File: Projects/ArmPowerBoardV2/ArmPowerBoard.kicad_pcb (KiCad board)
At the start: 2 copper layers, 130 x 65.2 mm, 14 parts, among them J1 22V Output, J2 12V Output, P1 BATT_CON, U1 IQL24040A050V-009-R-ND

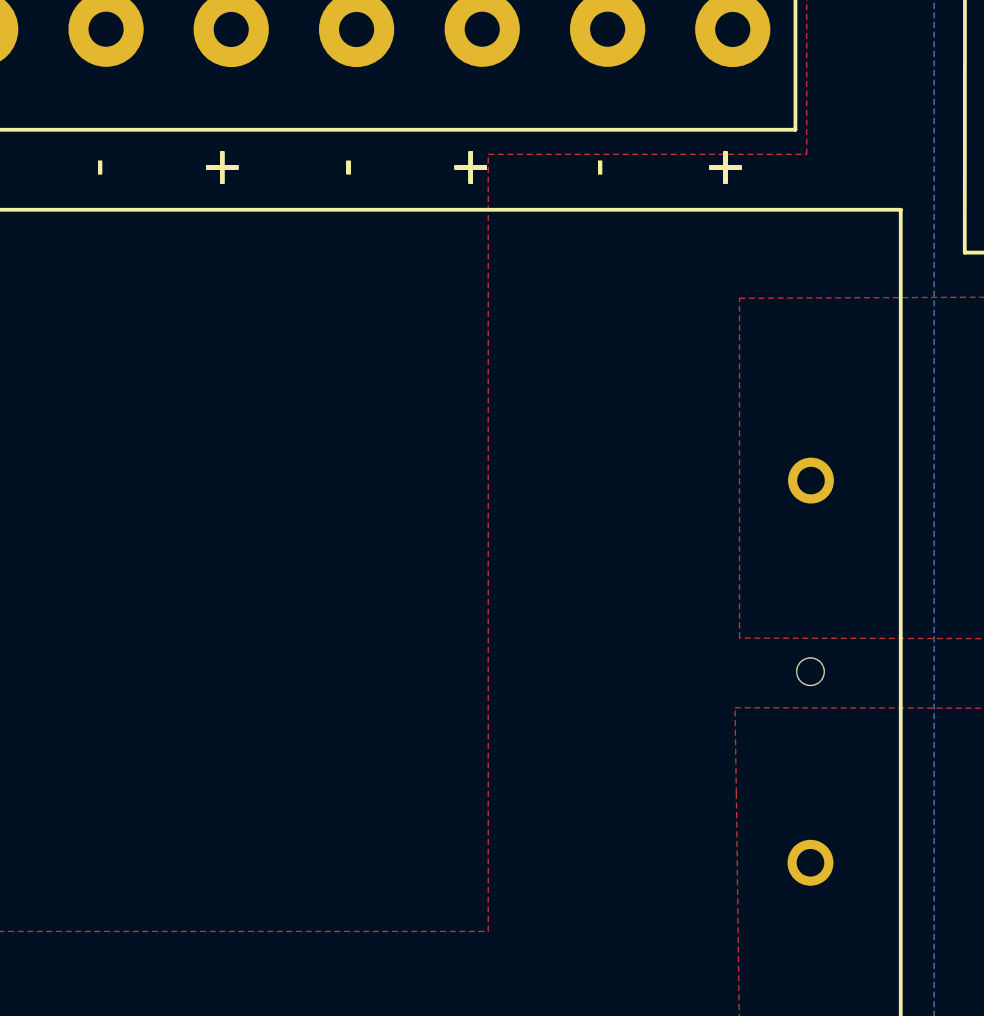
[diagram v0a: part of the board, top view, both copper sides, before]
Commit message: The on/off switch is conncted to power
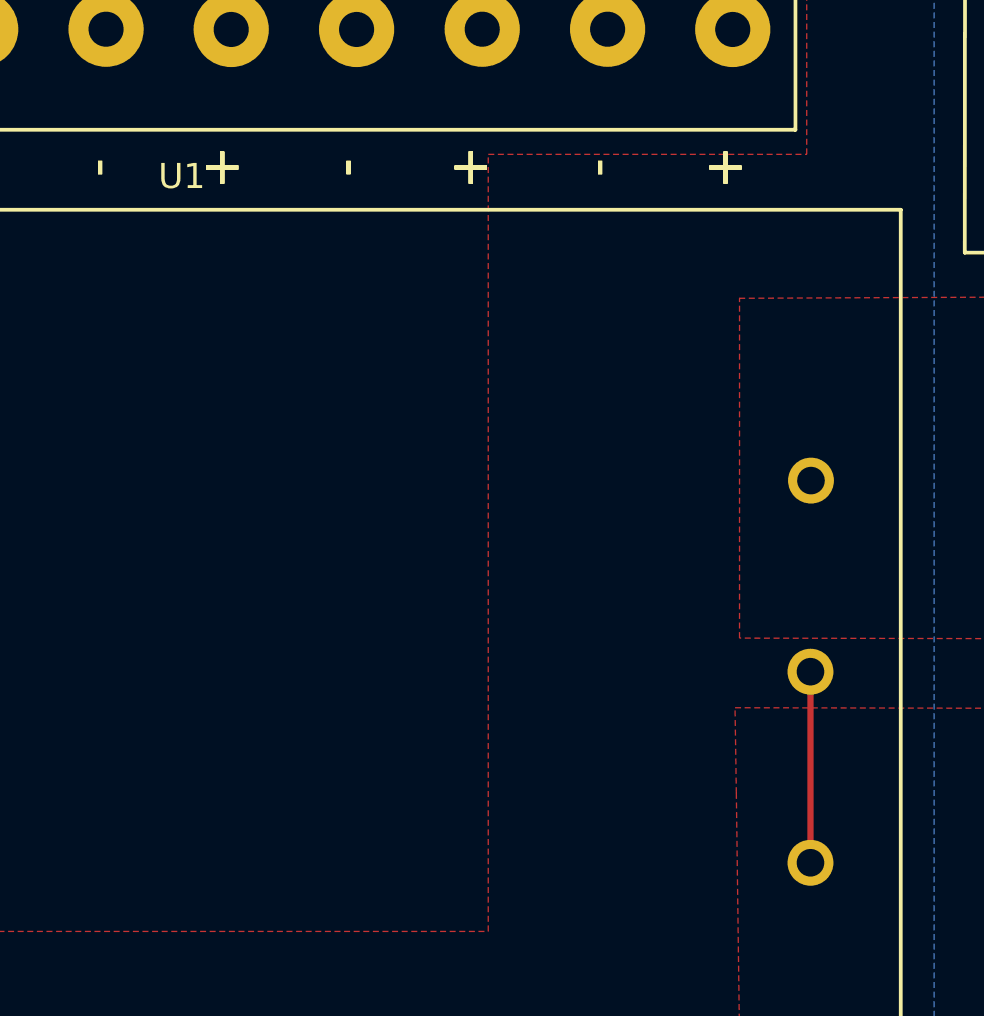
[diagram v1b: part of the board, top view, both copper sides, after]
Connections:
- 9.31kR pad 1: (no net) -> Net-(0.27-Pad2)
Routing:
- net Net-(P1-Pad2): track 0.00 -> 7.62 mm
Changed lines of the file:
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@@
 (kicad_pcb (version 4) (host pcbnew 4.0.7)
   (general
-    (links 0)
+    (links 52)
     (no_connects 0)
-    (area 48.224999 104.724999 178.375001 166.075001)
+    (area 48.224999 102.724999 178.375001 168.075001)
     (thickness 1.6)
     (drawings 33)
-    (tracks 103)
+    (tracks 105)
     (zones 0)
     (modules 14)
@@
     (mod_text_size 1 1)
     (mod_text_width 0.15)
-    (pad_size 3.2 3.2)
-    (pad_drill 3.2)
+    (pad_size 2.59 2.59)
+    (pad_drill 1.7)
     (pad_to_mask_clearance 0.2)
     (aux_axis_origin 0 0)
@@
       (net 6 "Net-(P1-Pad2)"))
   )
-  (module USST-footprints:IQL24040A050V_Power_Supply (layer F.Cu)
-    (at 81.1887 149.662 180)
-    (fp_text reference U1 (at -25.73 27.37 180) (layer F.SilkS) hide
-      (effects (font (size 1 1) (thickness 0.15)))
-    )
-    (fp_text value IQL24040A050V-009-R-ND (at -25.82 24.43 180) (layer F.Fab)
-      (effects (font (size 1 1) (thickness 0.15)))
-    )
-    (fp_line (start -54.36 -10.77) (end 3.6 -10.8) (layer F.SilkS) (width 0.15))
-    (fp_line (start 3.6 -10.8) (end 3.6 26.04) (layer F.SilkS) (width 0.15))
-    (fp_line (start 3.6 26.04) (end -54.4 26.04) (layer F.SilkS) (width 0.15))
-    (fp_line (start -54.4 26.04) (end -54.4 -10.8) (layer F.SilkS) (width 0.15))
-    (pad 8 thru_hole circle (at 0 0 180) (size 2.59 2.59) (drill 1.7) (layers *.Cu *.Mask)
-      (net 3 "Net-(0.27-Pad2)"))
-    (pad 4 thru_hole circle (at 0 15.29 180) (size 2.59 2.59) (drill 1.7) (layers *.Cu *.Mask)
-      (net 1 /-Vout))
-    (pad 7 thru_hole circle (at 0 3.81 180) (size 1.83 1.83) (drill 1.1) (layers *.Cu *.Mask)
-      (net 3 "Net-(0.27-Pad2)"))
-    (pad 6 thru_hole circle (at 0 7.62 180) (size 1.83 1.83) (drill 1.1) (layers *.Cu *.Mask)
-      (net 4 "Net-(9.3182-Pad2)"))
-    (pad 8 thru_hole circle (at 0 11.43 180) (size 1.83 1.83) (drill 1.1) (layers *.Cu *.Mask)
-      (net 3 "Net-(0.27-Pad2)"))
-    (pad 1 thru_hole circle (at -50.8 0 180) (size 1.83 1.83) (drill 1.1) (layers *.Cu *.Mask)
-      (net 6 "Net-(P1-Pad2)"))
-    (pad "" np_thru_hole circle (at -50.8 7.62 180) (size 1.1 1.1) (drill 1.1) (layers *.Cu *.Mask))
-    (pad 3 thru_hole circle (at -50.82 15.24 180) (size 1.83 1.83) (drill 1.1) (layers *.Cu *.Mask)
-      (net 5 GND))
-  )
   (module Resistors_SMD:R_1812 (layer F.Cu)
     (at 73.05984 132.904538)
@@
     (fp_line (start 0.6 0.875) (end -0.6 0.875) (layer F.SilkS) (width 0.15))
     (fp_line (start -0.6 -0.875) (end 0.6 -0.875) (layer F.SilkS) (width 0.15))
-    (pad 1 smd rect (at -0.95 0 90) (size 0.7 1.3) (layers F.Cu F.Paste F.Mask))
+    (pad 1 smd rect (at -0.95 0 90) (size 0.7 1.3) (layers F.Cu F.Paste F.Mask)
+      (net 3 "Net-(0.27-Pad2)"))
     (pad 2 smd rect (at 0.95 0 90) (size 0.7 1.3) (layers F.Cu F.Paste F.Mask)
       (net 4 "Net-(9.3182-Pad2)"))
@@
       (net 24 "Net-(USB1-Pad18)"))
   )
+  (module USST-footprints:IQL24040A050V_Power_Supply (layer F.Cu)
+    (at 81.1887 149.662 180)
+    (fp_text reference U1 (at -25.73 27.37 360) (layer F.SilkS)
+      (effects (font (size 1 1) (thickness 0.15)))
+    )
+    (fp_text value IQL24040A050V-009-R-ND (at -25.82 24.43 180) (layer F.Fab)
+      (effects (font (size 1 1) (thickness 0.15)))
+    )
+    (fp_line (start -54.36 -10.77) (end 3.6 -10.8) (layer F.SilkS) (width 0.15))
+    (fp_line (start 3.6 -10.8) (end 3.6 26.04) (layer F.SilkS) (width 0.15))
+    (fp_line (start 3.6 26.04) (end -54.4 26.04) (layer F.SilkS) (width 0.15))
+    (fp_line (start -54.4 26.04) (end -54.4 -10.8) (layer F.SilkS) (width 0.15))
+    (pad 8 thru_hole circle (at 0 0 180) (size 2.59 2.59) (drill 1.7) (layers *.Cu *.Mask)
+      (net 3 "Net-(0.27-Pad2)"))
+    (pad 4 thru_hole circle (at 0 15.29 180) (size 2.59 2.59) (drill 1.7) (layers *.Cu *.Mask)
+      (net 1 /-Vout))
+    (pad 7 thru_hole circle (at 0 3.81 180) (size 1.83 1.83) (drill 1.1) (layers *.Cu *.Mask)
+      (net 3 "Net-(0.27-Pad2)"))
+    (pad 6 thru_hole circle (at 0 7.62 180) (size 1.83 1.83) (drill 1.1) (layers *.Cu *.Mask)
+      (net 4 "Net-(9.3182-Pad2)"))
+    (pad 5 thru_hole circle (at 0 11.43 180) (size 1.83 1.83) (drill 1.1) (layers *.Cu *.Mask)
+      (net 1 /-Vout))
+    (pad 1 thru_hole circle (at -50.8 0 180) (size 1.83 1.83) (drill 1.1) (layers *.Cu *.Mask)
+      (net 6 "Net-(P1-Pad2)"))
+    (pad 2 thru_hole circle (at -50.8 7.62 180) (size 1.83 1.83) (drill 1.1) (layers *.Cu *.Mask)
+      (net 6 "Net-(P1-Pad2)"))
+    (pad 3 thru_hole circle (at -50.82 15.24 180) (size 1.83 1.83) (drill 1.1) (layers *.Cu *.Mask)
+      (net 5 GND))
+  )
   (gr_line (start 48.3 168) (end 178.3 168) (layer Edge.Cuts) (width 0.15))
   (gr_line (start 178.3 102.8) (end 48.3 102.8) (layer Edge.Cuts) (width 0.15))
@@
   (segment (start 81.1887 142.432) (end 74.749318 142.432) (width 0.25) (layer F.Cu) (net 4))
   (segment (start 74.749318 142.432) (end 74.038032 143.143286) (width 0.25) (layer F.Cu) (net 4))
+  (segment (start 131.9887 134.442) (end 132.0087 134.422) (width 0.25) (layer F.Cu) (net 5))
+  (segment (start 131.9887 142.042) (end 131.9887 149.662) (width 0.25) (layer F.Cu) (net 6))
   (segment (start 159.5339 114.9316) (end 159.5745 114.9722) (width 0.25) (layer F.Cu) (net 7))
   (segment (start 144.1616 114.9316) (end 159.5339 114.9316) (width 0.25) (layer F.Cu) (net 7))
